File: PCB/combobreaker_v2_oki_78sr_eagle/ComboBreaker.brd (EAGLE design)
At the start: 60.9 x 39.4 mm, 13 parts

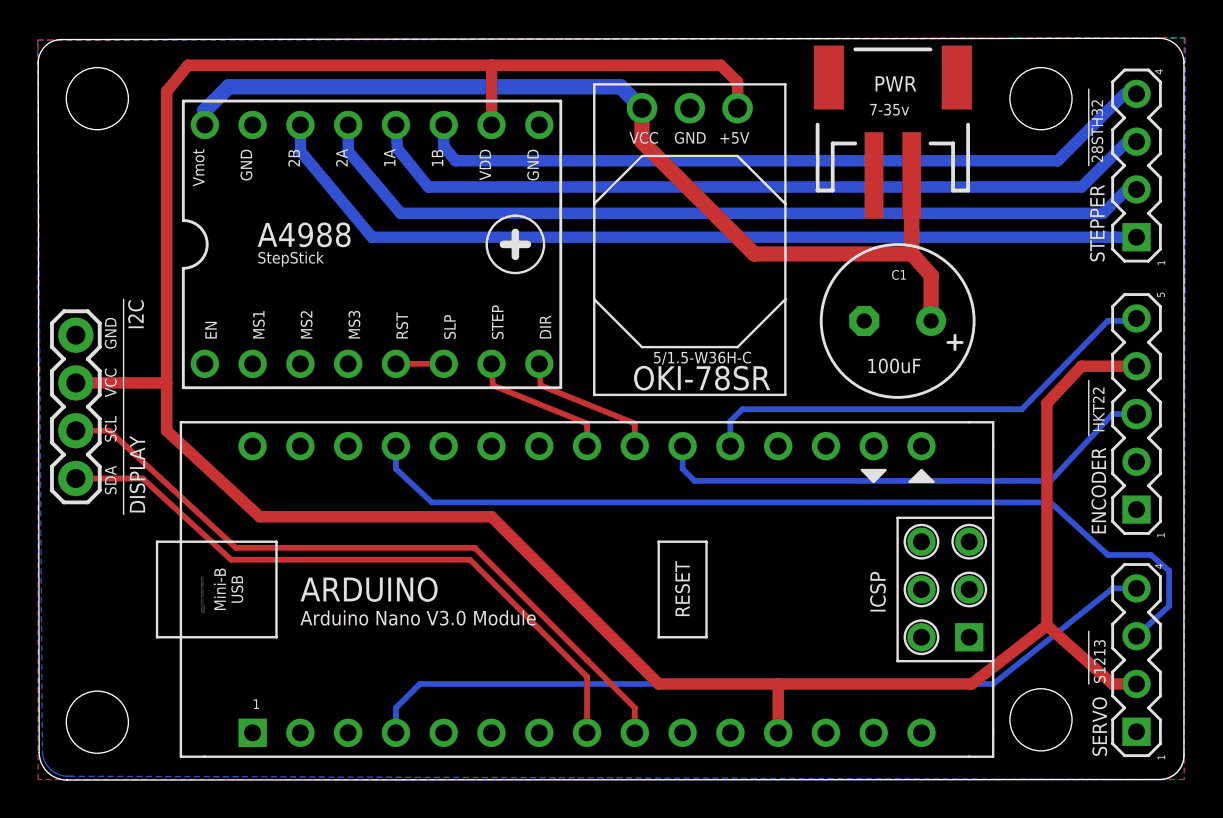
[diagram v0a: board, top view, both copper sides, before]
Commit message: Updated v2 Eagle PCB
* Added more silkscreen details
* Minor adjustments to footprints

TO-DO:
* Confirm pinout wire colors
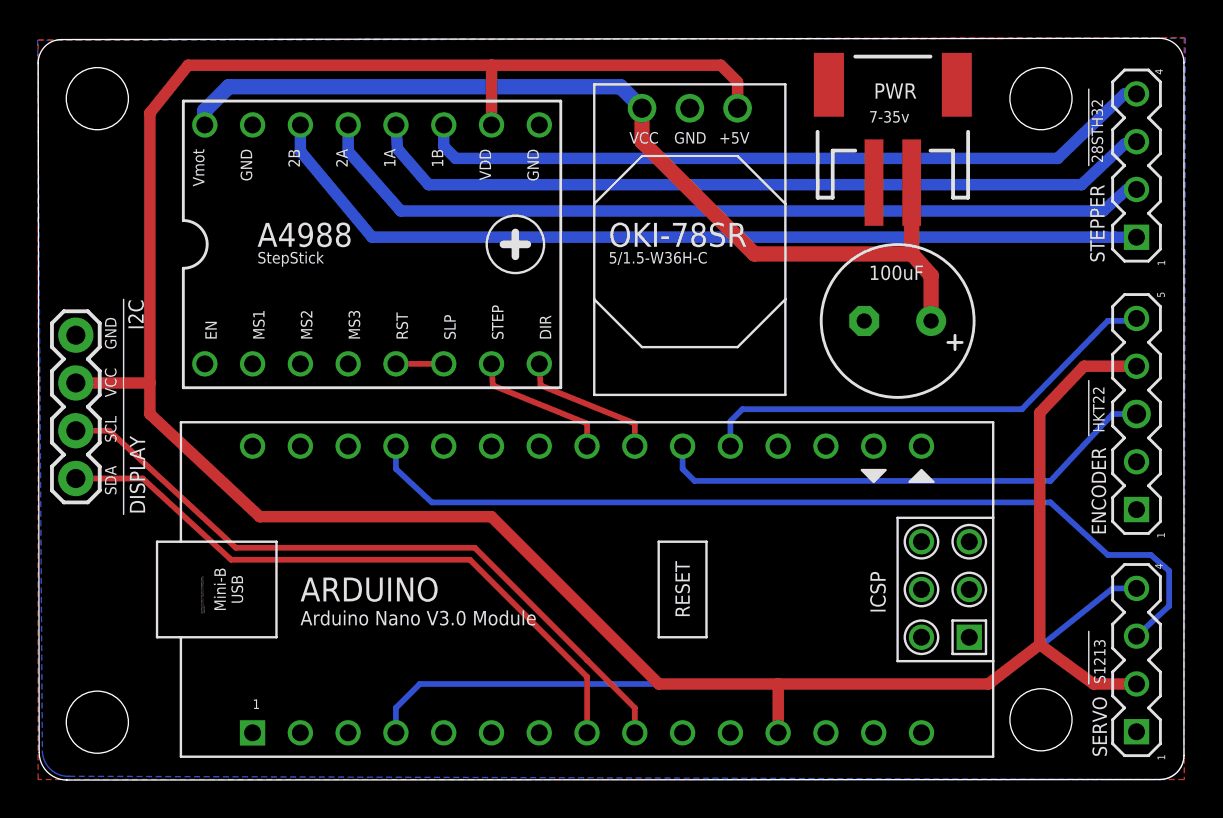
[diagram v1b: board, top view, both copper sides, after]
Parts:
- added U$5: (no value), Aidan:AM
- moved PWR 0.38 mm to (45.5, 35.4)
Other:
- board text added: "1> Black 2> Brown 3> Red 4> White"
- board text added: "Aidan McCarthy"
- board text added: "ComboBreaker!!!"
- board text added: "DESIGN:"
- board text added: "ENCODER"
- board text added: "PCB:"
- board text added: "SERVO"
- board text added: "STEPPER"
- board text added: "Samy Kamkar"

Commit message: Updated v2 Eagle PCB (Prototype Ordered!)
This is final prototype design sent to printers!

* Added Master Lock logo
* Added pinout wire colors to bottom silkscreen
* Added pin identifiers to servo/stepper/encoder pins on top silkscreen
* Redraw ground pour polygons
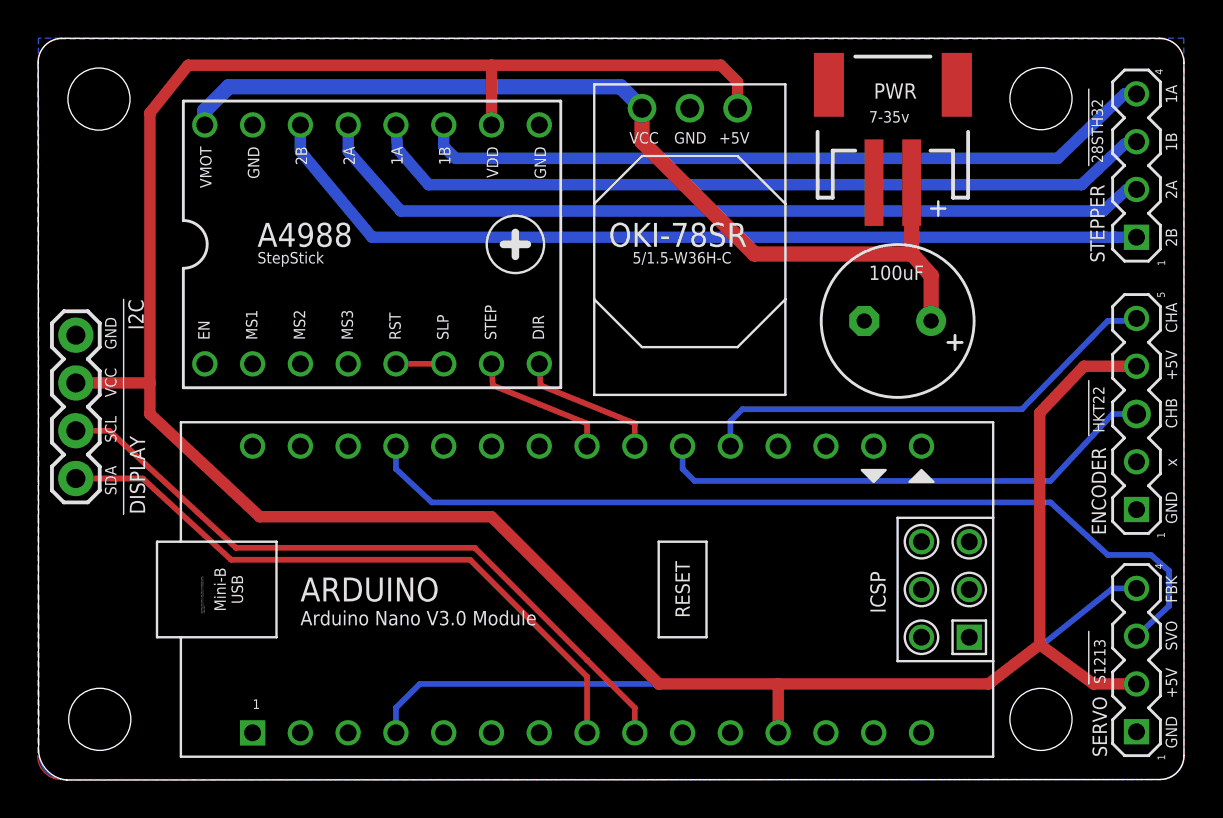
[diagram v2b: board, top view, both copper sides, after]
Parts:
- added U$6: (no value), Aidan:MASTERLOCK2
- moved U$1 0.20 mm to (3.30, 3.20)
- moved U$2 0.09 mm to (3.26, 36.2)
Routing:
- added copper zone on layer 1, net N$4
- removed copper zone on layer 1, net GND
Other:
- outline, holes or cut-outs redrawn
- board text added: "1> Black 2> Green 3> Brown 4> Red 5> White"
- board text added: "1> Blue 2> Red 3> Green 4> Black"
- board text added: "1> Brown 2> Red 3> Orange 4> White"
- board text added: "1A"
- board text added: "1B"
- board text added: "2A"
- board text added: "2B"
- board text added: "CHA"
- board text added: "CHB"
- board text added: "FBK"
- board text added: "SVO"
- board text added: "x"
- board text removed: "1> Black 2> Brown 3> Red 4> White"
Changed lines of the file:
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@@
 <setting verticaltext="up"/>
 </settings>
-<grid distance="0.05" unitdist="inch" unit="inch" style="lines" multiple="1" display="no" altdistance="0.005" altunitdist="inch" altunit="inch"/>
+<grid distance="0.05" unitdist="inch" unit="inch" style="lines" multiple="1" display="no" altdistance="0.000000123031" altunitdist="inch" altunit="inch"/>
 <layers>
 <layer number="1" name="Top" color="4" fill="1" visible="yes" active="yes"/>
@@
 <board>
 <plain>
-<wire x1="0.030275" y1="38.0949125" x2="0.083059375" y2="1.440609375" width="0" layer="20"/>
-<wire x1="0.083059375" y1="1.440609375" x2="1.55371875" y2="-0.027475" width="0" layer="20" curve="89.951882"/>
+<wire x1="0.030275" y1="38.0949125" x2="0.050884375" y2="1.794709375" width="0" layer="20"/>
+<wire x1="0.050884375" y1="1.794709375" x2="1.55371875" y2="-0.027475" width="0" layer="20" curve="89.951882"/>
 <wire x1="1.55371875" y1="-0.027475" x2="59.67" y2="-0.00064375" width="0" layer="20"/>
 <wire x1="59.67" y1="-0.00064375" x2="60.94" y2="1.27" width="0" layer="20" curve="89.890974"/>
 <wire x1="60.94" y1="1.27" x2="60.94" y2="38.100034375" width="0" layer="20"/>
 <wire x1="60.94" y1="38.100034375" x2="59.63313125" y2="39.40525" width="0" layer="20" curve="90.072431"/>
-<wire x1="59.63313125" y1="39.40525" x2="1.270040625" y2="39.337909375" width="0" layer="20"/>
-<wire x1="1.270040625" y1="39.337909375" x2="0.030275" y2="38.0949125" width="0" layer="20" curve="90.008361"/>
+<wire x1="59.63313125" y1="39.40525" x2="1.270040625" y2="39.405346875" width="0" layer="20"/>
+<wire x1="1.270040625" y1="39.405346875" x2="0.030275" y2="38.0949125" width="0" layer="20" curve="90.008361"/>
 <text x="4.191" y="15.113" size="0.6096" layer="21" rot="R90">SDA</text>
 <text x="4.191" y="17.907" size="0.6096" layer="21" rot="R90">SCL</text>
@@
 <wire x1="55.88" y1="5.08" x2="55.88" y2="7.874" width="0.0762" layer="21"/>
 <wire x1="4.572" y1="14.097" x2="4.572" y2="25.527" width="0.0762" layer="21"/>
-<text x="27.559" y="26.289" size="0.8128" layer="22" font="vector" rot="MR0">PCB:</text>
-<text x="24.257" y="26.289" size="1.27" layer="22" font="vector" ratio="20" rot="MR0">Aidan McCarthy</text>
-<text x="47.117" y="26.543" size="1.27" layer="22" font="vector" ratio="20" rot="MR0">Samy Kamkar</text>
-<text x="52.197" y="26.543" size="0.8128" layer="22" font="vector" rot="MR0">DESIGN:</text>
-<text x="52.324" y="28.321" size="3.81" layer="22" font="vector" ratio="20" rot="MR0">ComboBreaker!!!</text>
-<text x="43.307" y="12.319" size="1.27" layer="22" font="vector" ratio="20" rot="MR0">SERVO</text>
-<text x="42.672" y="7.112" size="0.8128" layer="22" font="vector" rot="MR0">1&gt; Black
-2&gt; Brown
-3&gt; Red
+<text x="25.146" y="26.543" size="0.8128" layer="22" font="vector" rot="MR0">PCB:</text>
+<text x="22.098" y="26.543" size="1.27" layer="22" font="vector" ratio="20" rot="MR0">Aidan McCarthy</text>
+<text x="44.958" y="26.543" size="1.27" layer="22" font="vector" ratio="20" rot="MR0">Samy Kamkar</text>
+<text x="50.165" y="26.543" size="0.8128" layer="22" font="vector" rot="MR0">DESIGN:</text>
+<text x="50.292" y="28.321" size="3.81" layer="22" font="vector" ratio="20" rot="MR0">ComboBreaker!!!</text>
+<text x="44.577" y="12.319" size="1.27" layer="22" font="vector" ratio="20" rot="MR0">SERVO</text>
+<text x="43.942" y="7.112" size="0.8128" layer="22" font="vector" rot="MR0">1&gt; Brown
+2&gt; Red
+3&gt; Orange
 4&gt; White</text>
 <text x="33.147" y="12.319" size="1.27" layer="22" font="vector" ratio="20" rot="MR0">ENCODER</text>
-<text x="32.512" y="7.112" size="0.8128" layer="22" font="vector" rot="MR0">1&gt; Black
-2&gt; Brown
-3&gt; Red
-4&gt; White</text>
+<text x="32.512" y="5.842" size="0.8128" layer="22" font="vector" rot="MR0">1&gt; Black
+2&gt; Green
+3&gt; Brown
+4&gt; Red
+5&gt; White</text>
 <text x="20.447" y="12.319" size="1.27" layer="22" font="vector" ratio="20" rot="MR0">STEPPER</text>
-<text x="19.812" y="7.112" size="0.8128" layer="22" font="vector" rot="MR0">1&gt; Black
-2&gt; Brown
-3&gt; Red
-4&gt; White</text>
+<text x="19.812" y="7.112" size="0.8128" layer="22" font="vector" rot="MR0">1&gt; Blue
+2&gt; Red
+3&gt; Green
+4&gt; Black</text>
+<text x="60.579" y="13.589" size="0.6096" layer="21" font="vector" rot="R90">GND</text>
+<text x="60.579" y="1.651" size="0.6096" layer="21" font="vector" rot="R90">GND</text>
+<text x="60.579" y="21.209" size="0.6096" layer="21" font="vector" rot="R90">+5V</text>
+<text x="60.579" y="4.318" size="0.6096" layer="21" font="vector" rot="R90">+5V</text>
+<text x="60.579" y="6.858" size="0.6096" layer="21" font="vector" rot="R90">SVO</text>
+<text x="60.579" y="9.398" size="0.6096" layer="21" font="vector" rot="R90">FBK</text>
+<text x="60.579" y="18.669" size="0.6096" layer="21" font="vector" rot="R90">CHB</text>
+<text x="60.579" y="23.749" size="0.6096" layer="21" font="vector" rot="R90">CHA</text>
+<text x="60.579" y="16.637" size="0.6096" layer="21" font="vector" rot="R90">x</text>
+<text x="60.579" y="30.861" size="0.6096" layer="21" font="vector" rot="R90">2A</text>
+<text x="60.579" y="28.321" size="0.6096" layer="21" font="vector" rot="R90">2B</text>
+<text x="60.579" y="33.401" size="0.6096" layer="21" font="vector" rot="R90">1B</text>
+<text x="60.579" y="35.941" size="0.6096" layer="21" font="vector" rot="R90">1A</text>
+<wire x1="47.879" y1="30.734" x2="47.879" y2="29.972" width="0.127" layer="21"/>
+<wire x1="48.26" y1="30.353" x2="47.498" y2="30.353" width="0.127" layer="21"/>
 </plain>
 <attributes>
@@
 <element name="OKI-78SR" library="carrilib" package="OKI-78SRH" value="5/1.5-W36H-C" x="34.671" y="25.527" smashed="yes" rot="R180">
 <attribute name="NAME" x="30.353" y="28.321" size="1.27" layer="21" ratio="10"/>
-<attribute name="VALUE" x="30.353" y="27.432" size="0.6096" layer="25"/>
+<attribute name="VALUE" x="31.623" y="27.432" size="0.6096" layer="25"/>
 </element>
 <element name="A4988" library="RepRapjr" package="A4988BREAKOUT" value="StepStick" x="19.05" y="28.448" smashed="yes" rot="R90">
@@
 <attribute name="VALUE" x="4.826" y="25.527" size="0.8128" layer="21" font="vector" ratio="15" rot="R270"/>
 </element>
-<element name="U$1" library="SparkFun-Hardware" package="STAND-OFF" value="" x="3.175" y="3.048" smashed="yes">
-<attribute name="VALUE" x="3.175" y="1.016" size="0.6096" layer="27" font="vector" ratio="20" align="top-center"/>
-</element>
-<element name="U$2" library="SparkFun-Hardware" package="STAND-OFF" value="" x="3.175" y="36.195" smashed="yes">
-<attribute name="VALUE" x="3.175" y="34.163" size="0.6096" layer="27" font="vector" ratio="20" align="top-center"/>
+<element name="U$1" library="SparkFun-Hardware" package="STAND-OFF" value="" x="3.304796875" y="3.19950625" smashed="yes">
+<attribute name="VALUE" x="3.304796875" y="1.16750625" size="0.6096" layer="27" font="vector" ratio="20" align="top-center"/>
+</element>
+<element name="U$2" library="SparkFun-Hardware" package="STAND-OFF" value="" x="3.26153125" y="36.17335625" smashed="yes">
+<attribute name="VALUE" x="3.26153125" y="34.14135625" size="0.6096" layer="27" font="vector" ratio="20" align="top-center"/>
 </element>
 <element name="U$3" library="SparkFun-Hardware" package="STAND-OFF" value="" x="53.34" y="36.195" smashed="yes">
 <attribute name="VALUE" x="53.34" y="34.163" size="0.6096" layer="27" font="vector" ratio="20" align="top-center"/>
 </element>
-<element name="U$4" library="SparkFun-Hardware" package="STAND-OFF" value="" x="53.34" y="3.175" smashed="yes">
-<attribute name="VALUE" x="53.34" y="1.143" size="0.6096" layer="27" font="vector" ratio="20" align="top-center"/>
+<element name="U$4" library="SparkFun-Hardware" package="STAND-OFF" value="" x="53.34" y="3.19664375" smashed="yes">
+<attribute name="VALUE" x="53.34" y="1.16464375" size="0.6096" layer="27" font="vector" ratio="20" align="top-center"/>
 </element>
 <element name="U$5" library="Aidan" package="AM" value="" x="52.832" y="27.813" rot="R90"/>
+<element name="U$6" library="Aidan" package="MASTERLOCK2" value="" x="48.133" y="33.02" rot="MR0"/>
 </elements>
 <signals>
@@
 <signal name="GND">
 <polygon width="0.4064" layer="16">
-<vertex x="61.0164375" y="39.41236875"/>
-<vertex x="0.00038125" y="39.299490625"/>
-<vertex x="0.25438125" y="1.4717" curve="90.08677"/>
-<vertex x="1.6837375" y="0.172084375"/>
+<vertex x="60.96180625" y="1.3426625"/>
+<vertex x="60.926571875" y="39.41236875"/>
+<vertex x="0.045315625" y="39.4118875"/>
+<vertex x="0.074646875" y="1.291865625" curve="90.08677"/>
+<vertex x="1.504003125" y="-0.00775"/>
 <vertex x="59.61815" y="-0.002034375" curve="89.906409"/>
-<vertex x="60.96180625" y="1.3426625"/>
-</polygon>
-<polygon width="0.4064" layer="1">
-<vertex x="0.028603125" y="39.313584375"/>
-<vertex x="60.96" y="39.4405875"/>
-<vertex x="60.96" y="0"/>
-<vertex x="0.02860625" y="-0.000003125" curve="-225"/>
-<vertex x="0.028603125" y="0"/>
 </polygon>
 <contactref element="ENCODER" pad="1"/>
@@
 <contactref element="PWR" pad="1"/>
 <contactref element="DISPLAY" pad="1"/>
+<wire x1="43.94388125" y1="24.3779" x2="44.466" y2="31.733" width="0" layer="19" extent="1-1"/>
 </signal>
 <signal name="2A_RED">
@@
 <wire x1="23.241" y1="12.319" x2="10.541" y2="12.319" width="0.3048" layer="1"/>
 </signal>
+<signal name="N$4">
+<polygon width="0.4064" layer="1">
+<vertex x="0" y="13.97"/>
+<vertex x="0" y="1.27" curve="90"/>
+<vertex x="1.27" y="0"/>
+<vertex x="59.69" y="0" curve="90"/>
+<vertex x="60.96" y="1.27"/>
+<vertex x="60.96" y="38.1" curve="90"/>
+<vertex x="59.69" y="39.37"/>
+<vertex x="1.27" y="39.37" curve="90"/>
+<vertex x="0" y="38.1"/>
+</polygon>
+</signal>
 </signals>
